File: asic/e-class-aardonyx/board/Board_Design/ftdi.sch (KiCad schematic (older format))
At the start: 62 parts, among them J1 USB_B_6PIN, J17 USB_OTG, J18 Conn_1x3_M, J2 Conn_1x8, J3 Conn_1x3_M, U1 FT2232H, U16 93LC56BT-I_OT, Y1 12MHz

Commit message: Updating layout
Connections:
- net TCK: now also J2.2 (Pin_2), R5.2, R6.1; no longer J2.3 (Pin_3), R7.2, R8.1
- net TDI: now also J2.5 (Pin_5), R15.2, R16.1; no longer J2.6 (Pin_6), R17.2, R18.1
- net TDO: now also J2.6 (Pin_6), R17.2, R18.1; no longer J2.5 (Pin_5), R15.2, R16.1
- net TRST: now also J2.3 (Pin_3), R7.2, R8.1; no longer J2.2 (Pin_2), R5.2, R6.1
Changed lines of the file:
@@
 	3800 4450 4100 4450
 Connection ~ 3800 4450
-Text Label 9300 3450 0    39   ~ 0
-TMS
-Text Label 9300 3550 0    39   ~ 0
-TDO
 $Comp
 L Aardonyx-rescue:R_US-aardonyx R5
@@
 $EndComp
 Wire Wire Line
-	9750 3250 9750 3150
-Connection ~ 9750 3250
-Wire Wire Line
-	9750 3250 9750 3750
-Wire Wire Line
-	10000 3150 10000 3350
-Connection ~ 10000 3350
-Wire Wire Line
-	10000 3350 10000 3750
-Wire Wire Line
 	9300 3650 10750 3650
 Connection ~ 10750 3650
@@
 	10500 3550 10500 3750
 Wire Wire Line
-	9300 3450 10250 3450
-Wire Wire Line
-	10250 3450 10250 3750
-Wire Wire Line
 	10500 3150 10500 3550
-Wire Wire Line
-	10250 3450 10250 3150
-Connection ~ 10250 3450
 Wire Wire Line
 	9750 2850 9750 2800
@@
 Wire Wire Line
 	9300 3550 10500 3550
-Wire Wire Line
-	9300 3350 10000 3350
-Wire Wire Line
-	9300 3250 9750 3250
 Wire Wire Line
 	6850 2650 7350 2650
@@
 Wire Wire Line
 	3300 2450 3300 2350
-Text Label 9300 3350 0    39   ~ 0
-TCK
 Text Label 4050 3750 0    50   ~ 0
 D+
@@
 Text Label 2100 3650 0    50   ~ 0
 USB_D-
-Text Label 9300 3650 0    39   ~ 0
+Wire Wire Line
+	9750 3150 9750 3250
+Wire Wire Line
+	9300 3250 9750 3250
+Connection ~ 9750 3250
+Text Label 9500 3250 2    50   ~ 0
+TCK
+Wire Wire Line
+	10000 3150 10000 3350
+Wire Wire Line
+	10000 3350 9300 3350
+Connection ~ 10000 3350
+Wire Wire Line
+	10000 3350 10000 3750
+Text Label 9500 3350 2    50   ~ 0
+TRST
+Wire Wire Line
+	9750 3250 9750 3750
+Wire Wire Line
+	10250 3150 10250 3450
+Wire Wire Line
+	9300 3450 10250 3450
+Connection ~ 10250 3450
+Wire Wire Line
+	10250 3450 10250 3750
+Text Label 9450 3450 2    50   ~ 0
+TMS
+Text Label 9450 3550 2    50   ~ 0
 TDI
-Text Label 9300 3250 0    39   ~ 0
-TRST
+Text Label 9500 3650 2    50   ~ 0
+TDO
 $EndSCHEMATC

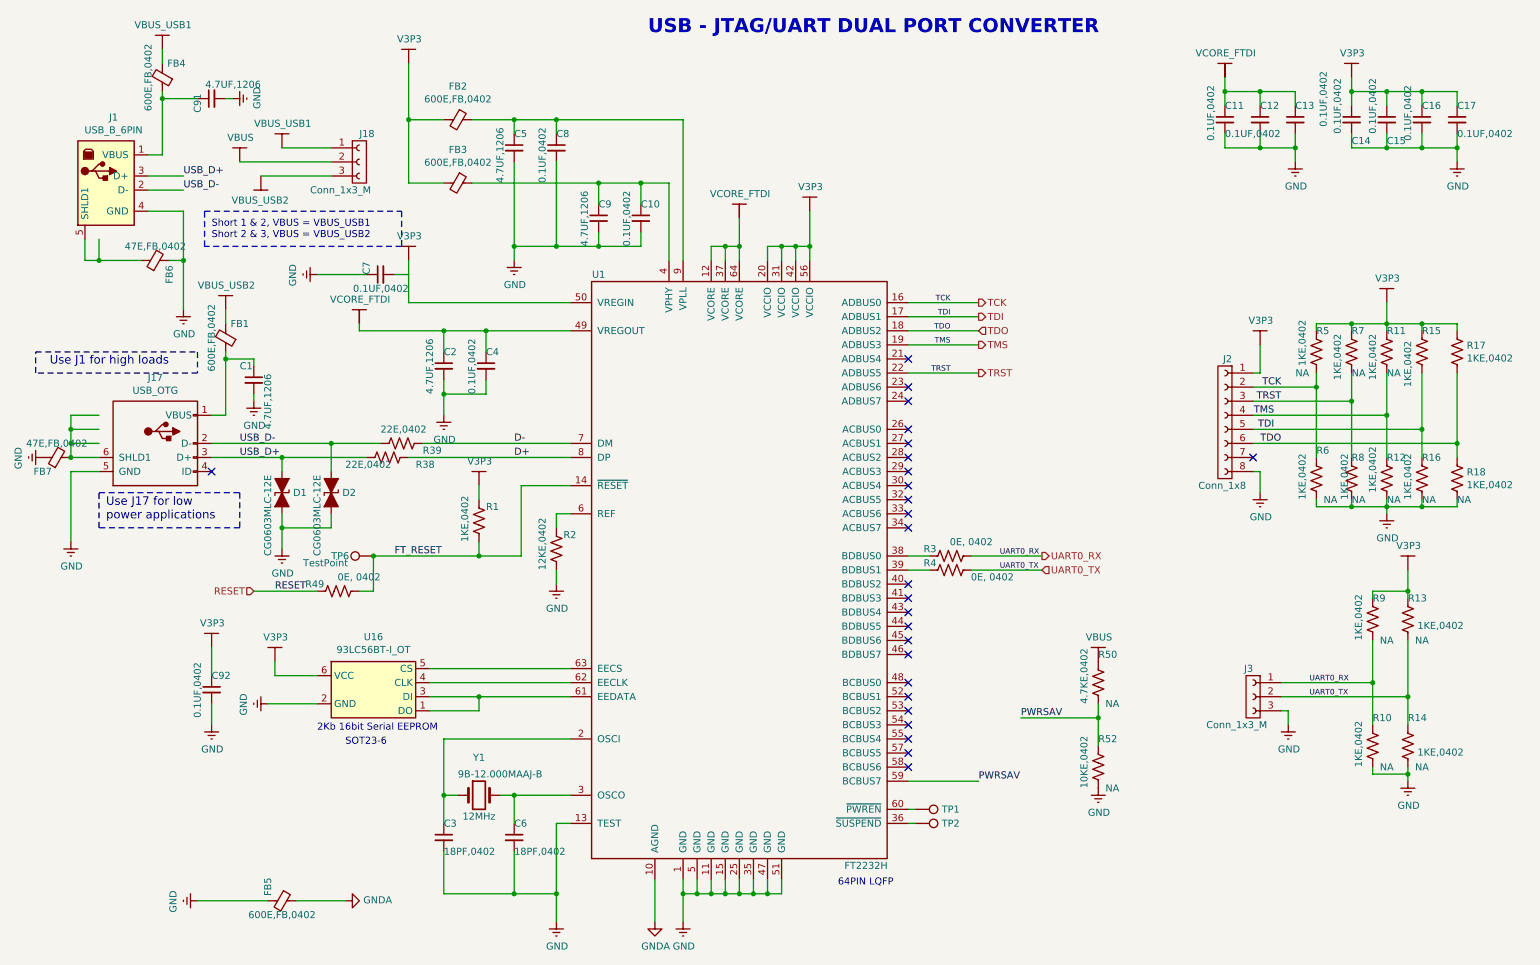
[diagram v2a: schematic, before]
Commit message: Updating layout after back annotation
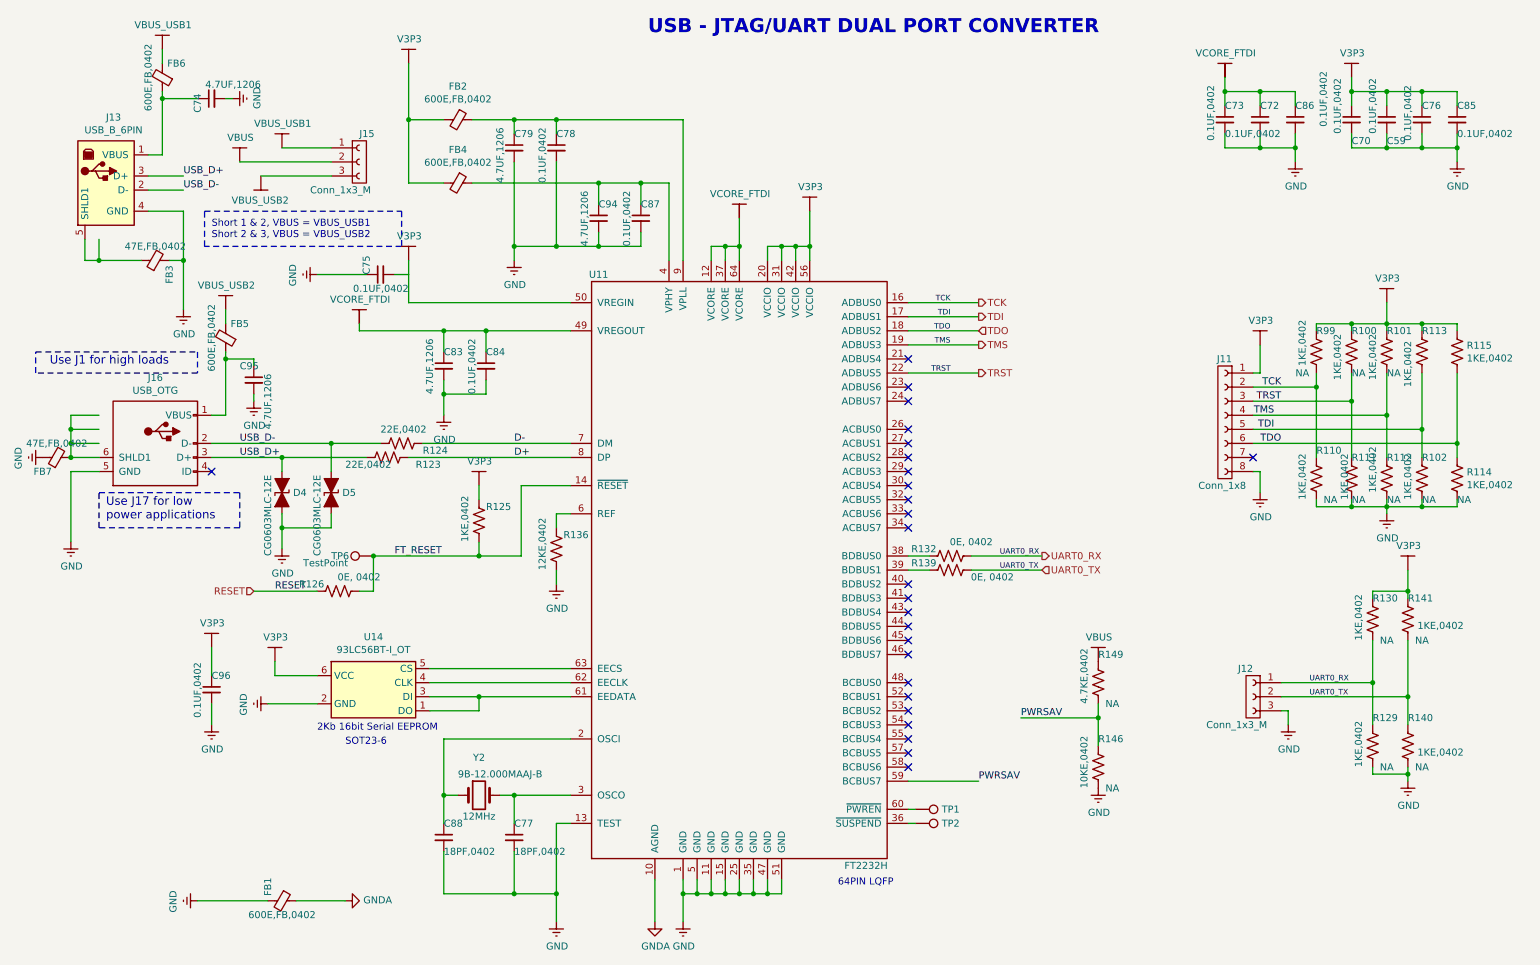
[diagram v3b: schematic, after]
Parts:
- renumbered C15 to C59, C14 to C70, C12 to C72, C11 to C73, C91 to C74, C7 to C75, C16 to C76, C6 to C77, C8 to C78, C5 to C79, C2 to C83, C4 to C84, C17 to C85, C13 to C86, C10 to C87, C3 to C88, C9 to C94, C1 to C95, C92 to C96, D1 to D4, D2 to D5, FB5 to FB1, FB6 to FB3, FB3 to FB4, FB1 to FB5, FB4 to FB6, J2 to J11, J3 to J12, J1 to J13, J18 to J15, J17 to J16, R7 to R100, R11 to R101, R16 to R102, R6 to R110, R8 to R111, R12 to R112, R15 to R113, R18 to R114, R17 to R115, R38 to R123, R39 to R124, R1 to R125, R49 to R126, R10 to R129, R9 to R130, R3 to R132, R2 to R136, R4 to R139, R14 to R140, R13 to R141, R52 to R146, R50 to R149, R5 to R99, U1 to U11, U16 to U14, Y1 to Y2

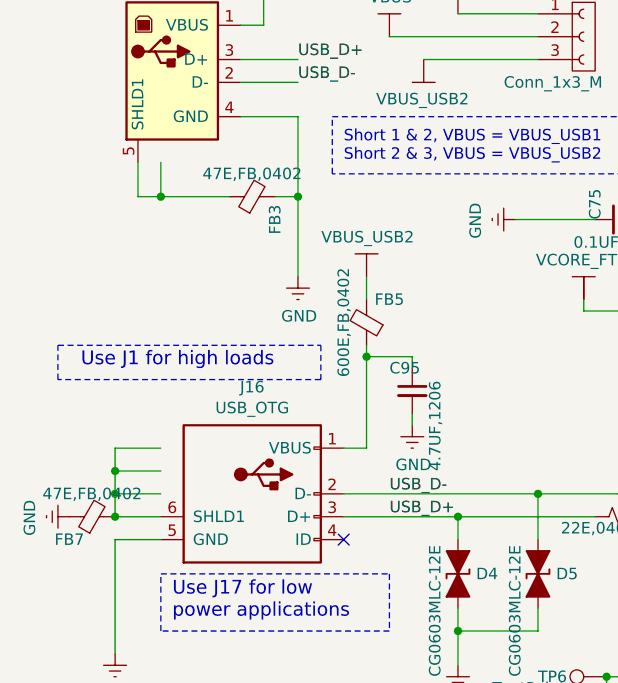
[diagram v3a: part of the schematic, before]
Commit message: Updating symbols for USB
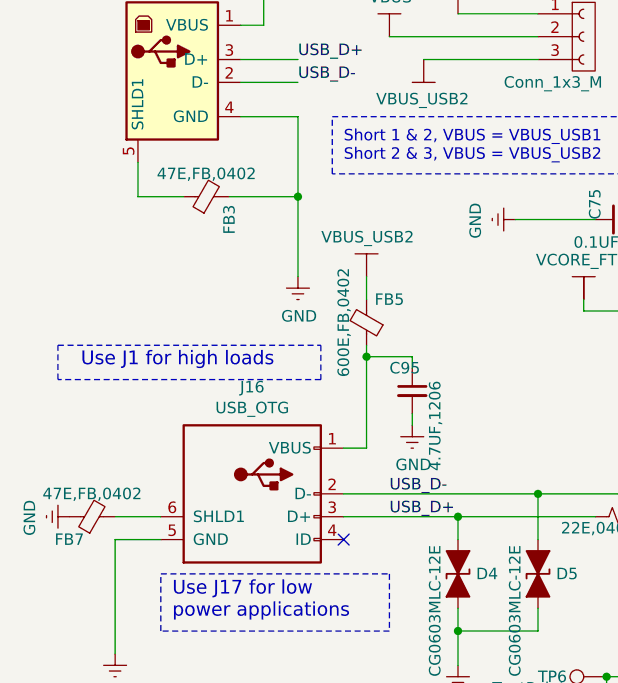
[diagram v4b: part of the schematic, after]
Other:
- moved on the sheet: FB3
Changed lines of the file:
@@
 $EndComp
-Wire Wire Line
-	1100 3450 900  3450
-Wire Wire Line
-	900  3450 900  3550
-Wire Wire Line
-	1100 3550 900  3550
-Connection ~ 900  3550
-Wire Wire Line
-	900  3550 900  3650
-Wire Wire Line
-	1100 3650 900  3650
-Connection ~ 900  3650
-Wire Wire Line
-	900  3650 900  3750
 Wire Wire Line
 	1100 3750 900  3750
@@
 Wire Wire Line
 	1700 2000 1700 2350
-Wire Wire Line
-	1100 2200 1100 2350
-Wire Wire Line
-	1100 2350 1000 2350
 Wire Wire Line
 	1550 1200 1800 1200
@@
 	0    -1   -1   0
 $EndComp
-Connection ~ 1100 2350
 $Comp
 L Aardonyx-rescue:Ferrite_Bead_Small-aardonyx FB3
 U 1 1 5EF19677
-P 1500 2350
-F 0 "FB3" H 1400 2250 50  0000 C CNN
-F 1 "47E,FB,0402" V 1600 2350 50  0000 C CNN
-F 2 "Inductor_SMD:L_0402_1005Metric" V 1430 2350 50  0001 C CNN
-F 3 "https://www.digikey.in/product-detail/en/w%C3%BCrth-elektronik/742792608/732-1596-1-ND/1639540" H 1500 2350 50  0001 C CNN
-F 4 "FERRITE BEAD 47 OHM 0603 1LN" H 1500 2350 50  0001 C CNN "Description"
-F 5 "732-1596-1-ND" H 1500 2350 50  0001 C CNN "Digikey PartNumber"
-F 6 "742792608" H 1500 2350 50  0001 C CNN "Manufactured Part Number"
-F 7 "Wurth Elektronik" H 1500 2350 50  0001 C CNN "Maufaturer"
-	1    1500 2350
+P 1300 2350
+F 0 "FB3" H 1200 2250 50  0000 C CNN
+F 1 "47E,FB,0402" V 1400 2350 50  0000 C CNN
+F 2 "Inductor_SMD:L_0402_1005Metric" V 1230 2350 50  0001 C CNN
+F 3 "https://www.digikey.in/product-detail/en/w%C3%BCrth-elektronik/742792608/732-1596-1-ND/1639540" H 1300 2350 50  0001 C CNN
+F 4 "FERRITE BEAD 47 OHM 0603 1LN" H 1300 2350 50  0001 C CNN "Description"
+F 5 "732-1596-1-ND" H 1300 2350 50  0001 C CNN "Digikey PartNumber"
+F 6 "742792608" H 1300 2350 50  0001 C CNN "Manufactured Part Number"
+F 7 "Wurth Elektronik" H 1300 2350 50  0001 C CNN "Maufaturer"
+	1    1300 2350
 	0    -1   -1   0
 $EndComp
 Wire Wire Line
-	1100 2350 1400 2350
-Wire Wire Line
 	1450 2000 1700 2000
 Wire Wire Line
-	1600 2350 1700 2350
-Connection ~ 900  3750
+	1400 2350 1700 2350
 $Comp
 L Aardonyx-rescue:GND-aardonyx #PWR0168
@@
 Text Label 9500 3650 2    50   ~ 0
 TDO
+Wire Wire Line
+	1000 2350 1200 2350
 $EndSCHEMATC
